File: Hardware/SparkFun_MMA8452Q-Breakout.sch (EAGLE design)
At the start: 16 parts, among them U1 MMA8452Q

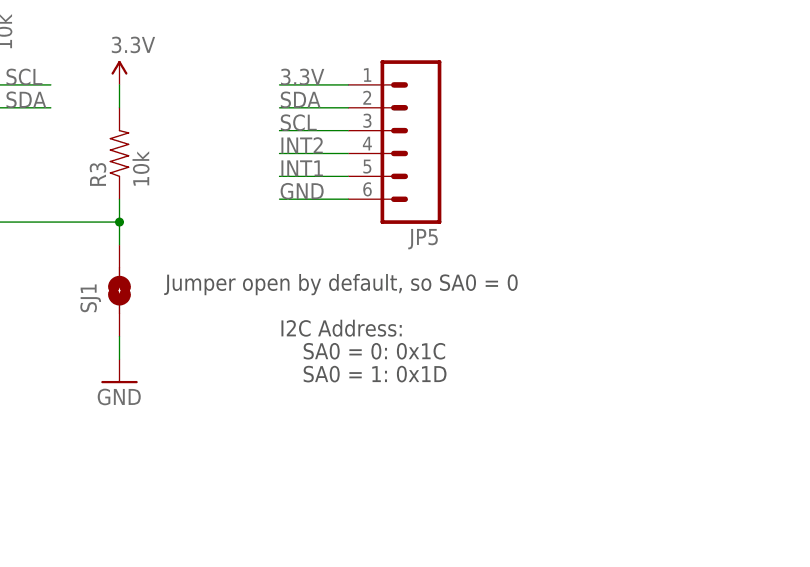
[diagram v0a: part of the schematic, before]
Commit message: Fixing I2C address on schematic
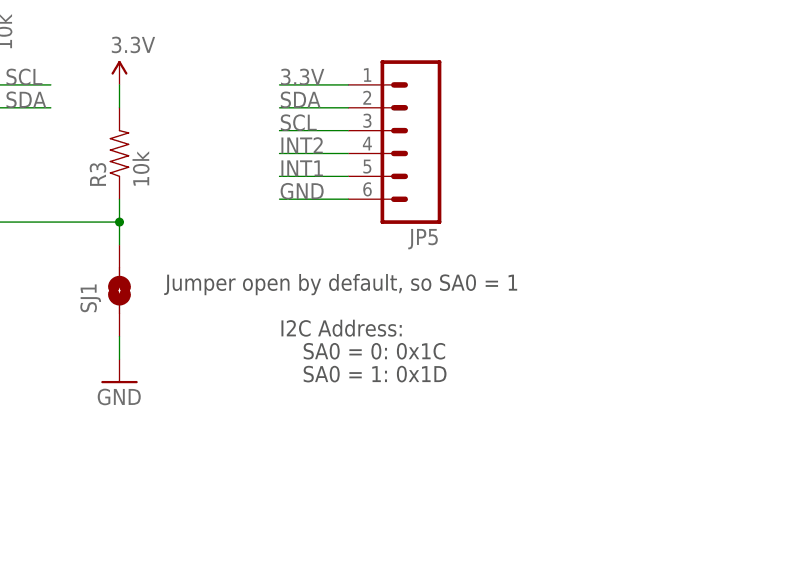
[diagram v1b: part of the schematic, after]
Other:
- note added: "Jumper open by default, so SA0 = 1"
- note removed: "Jumper open by default, so SA0 = 0"
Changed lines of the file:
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@@
 <?xml version="1.0" encoding="utf-8"?>
 <!DOCTYPE eagle SYSTEM "eagle.dtd">
-<eagle version="7.2.0">
+<eagle version="7.3.0">
 <drawing>
 <settings>
@@
 <text x="5.08" y="48.26" size="1.778" layer="97">* Changed the jumper configuration, single instead of 2-way</text>
 <text x="5.08" y="45.72" size="1.778" layer="97">* Minor adjustments to some silk, flipped axis + direction</text>
-<text x="167.64" y="83.82" size="1.778" layer="97">Jumper open by default, so SA0 = 0</text>
+<text x="167.64" y="83.82" size="1.778" layer="97">Jumper open by default, so SA0 = 1</text>
 <text x="236.22" y="7.62" size="3.81" layer="94">v11</text>
 </plain>
